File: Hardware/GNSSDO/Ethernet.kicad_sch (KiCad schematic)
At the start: 31 parts, among them J5 MagJack_PoE, U4 KSZ8041NL/I

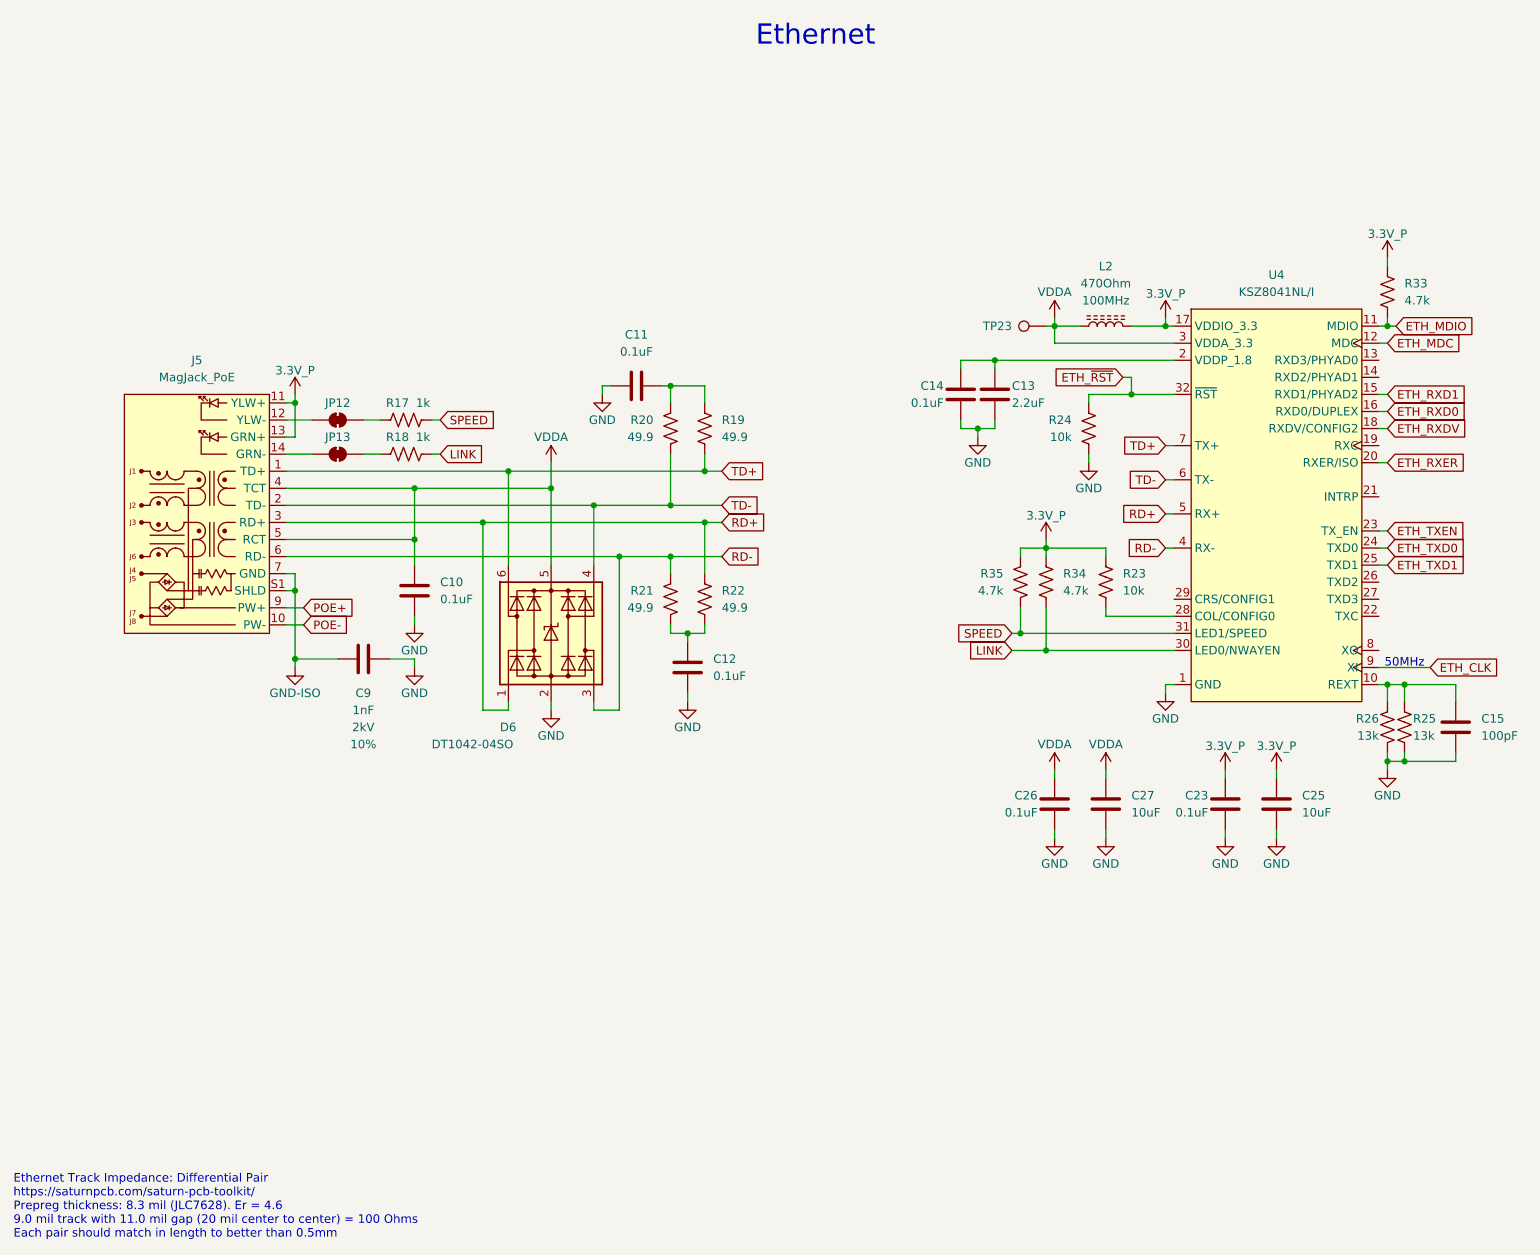
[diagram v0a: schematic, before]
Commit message: KiCad 10
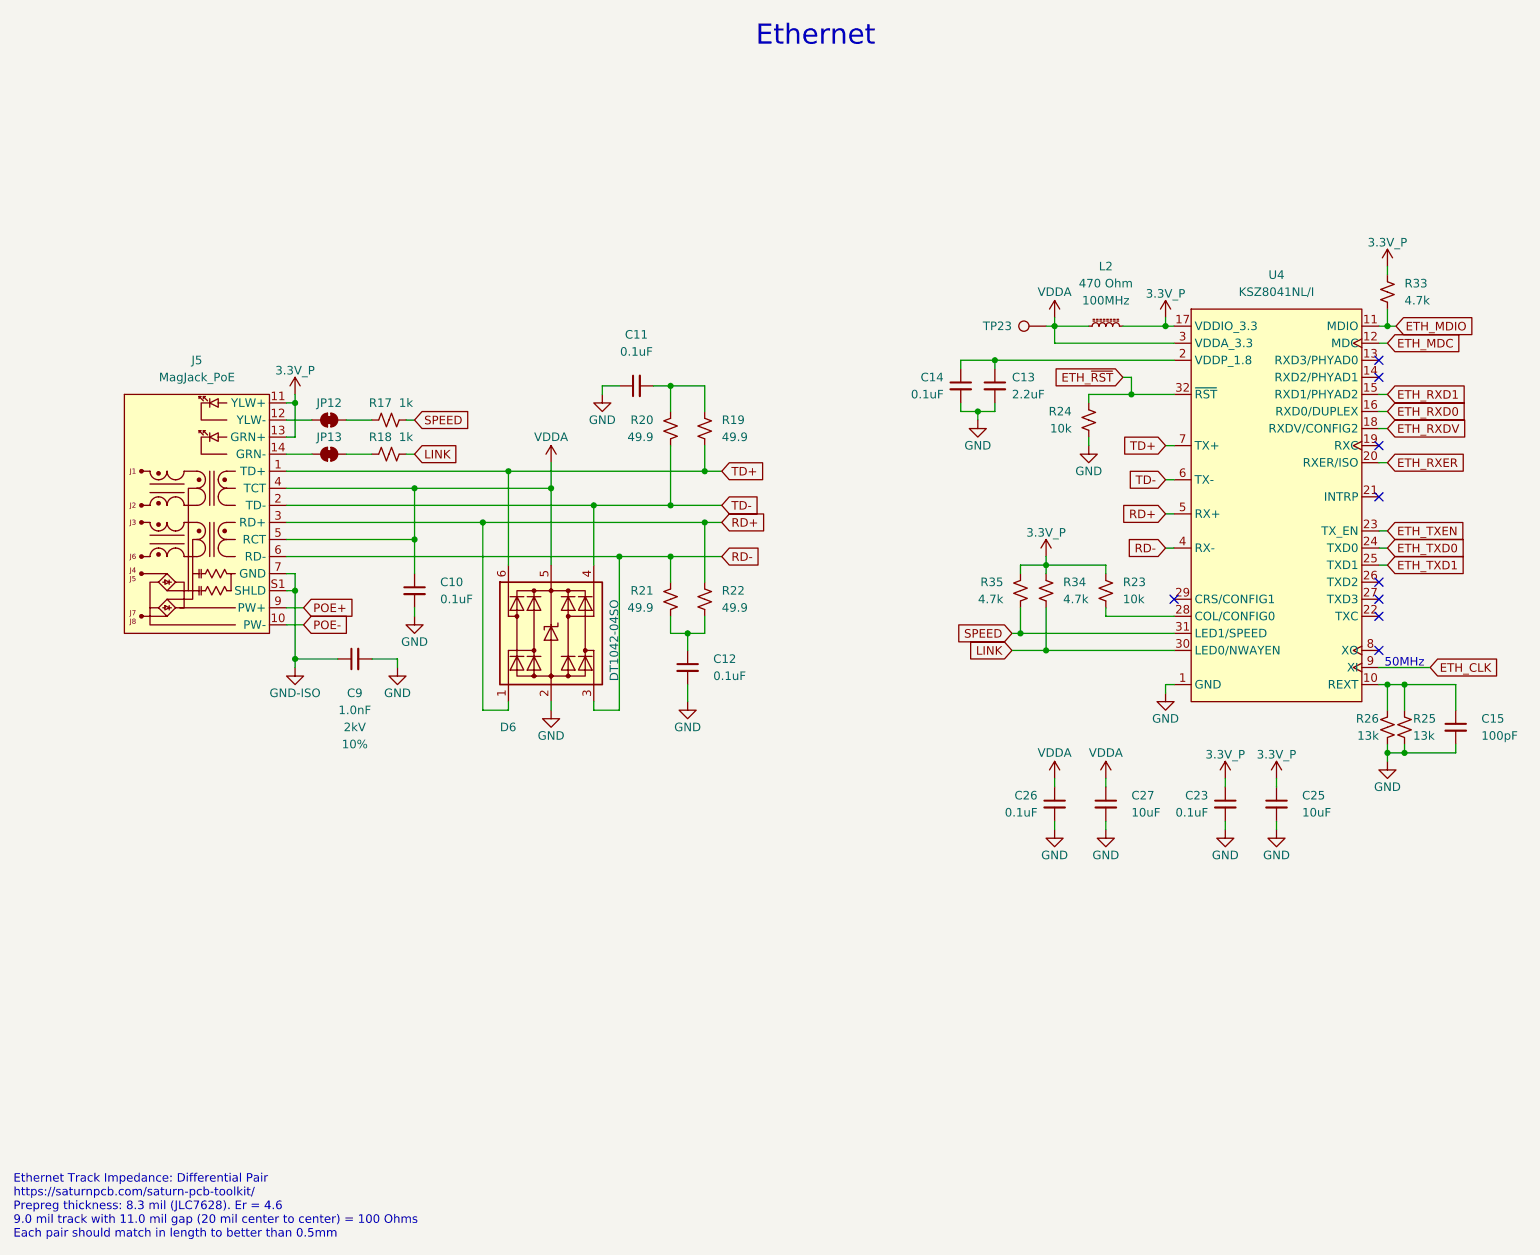
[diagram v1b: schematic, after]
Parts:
- C13: PROD_ID CAP-07888 -> CAP-24999
- C9: value 1nF -> 1.0nF
- D6: symbol SparkFun-DiscreteSemi:D_TVS_ESD_USB -> SparkFun-DiscreteSemi:D_TVS_ESD_USB_5V; Rating (none) -> 5VWM/9VC
- J5: symbol SparkFun-Connector:MagJack_PoE_RJ45 -> SparkFun-Connector:RJ45_MagJack_PoE
- JP12, JP13: value ~ -> (none)
- L2: value 470Ohm -> 470 Ohm; symbol SparkFun-Coil:470Ohm_0603_1.0A -> SparkFun-Coil:Ferrite_470Ohm_0603_1.0A
- TP23: footprint SparkFun-Connector:1x01 -> SparkFun-Connector:1x01_P2.54mm
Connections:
- net 3.3V_P: now also R23.1, R33.2, R34.2, R35.2; no longer R23.2, R33.1, R34.1, R35.1
- net ETH_MDIO: now also R33.1; no longer R33.2
- net ETH_~{RST}: now also R24.2; no longer R24.1
- net GND: now also R24.1, R25.1, R26.1; no longer R24.2, R25.2, R26.2
- net LINK: now also R18.2, R34.1; no longer R18.1, R34.2
- net RD+: now also R22.2; no longer R22.1
- net RD-: now also R21.2; no longer R21.1
- net SPEED: now also R17.2, R35.1; no longer R17.1, R35.2
- net TD+: now also R19.1; no longer R19.2
- net TD-: now also R20.1; no longer R20.2
- net at C15.1, U4.10 (REXT): now also R25.2, R26.2; no longer R25.1, R26.1
- net at JP13.2 (B): now also R18.1; no longer R18.2
- net at U4.28 (COL/CONFIG0): now also R23.2; no longer R23.1
- net at JP12.2 (B): now also R17.1; no longer R17.2
- new net: C12.1, R21.1, R22.1
- new net: C11.2, R19.2, R20.2
- no-connect marks 0 -> 9
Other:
- moved on the sheet: C13, C14, C9, JP12, JP13
